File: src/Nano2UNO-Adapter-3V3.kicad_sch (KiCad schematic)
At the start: 13 parts, among them J1 ESW-108-33-L-S, J2 ESW-110-33-L-S, J3 ESW-108-33-L-S, J4 ESW-106-33-L-S, J5 PPPC151LFBN-RC, J6 PPPC151LFBN-RC, J7 TSW-103-15-L-D, J8 PJ-102A, SW1 1825910-6, U1 R-78K5.0-0.5

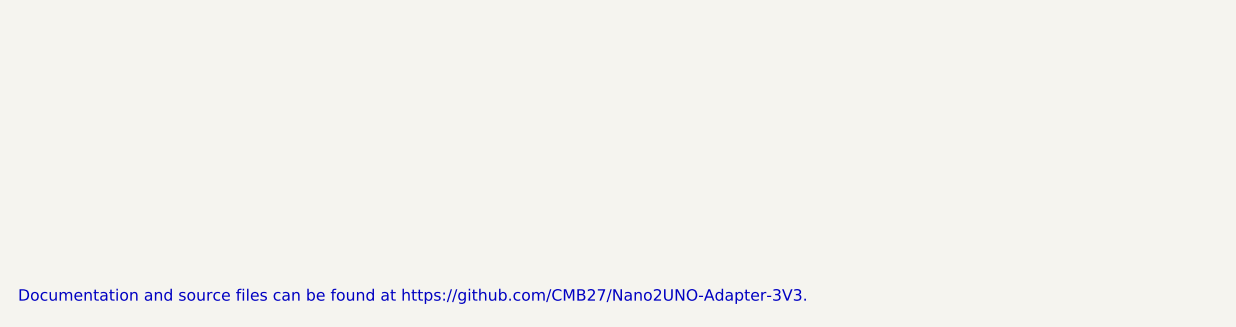
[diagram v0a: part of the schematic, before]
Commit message: Increased the font size of the comments and dimensions.
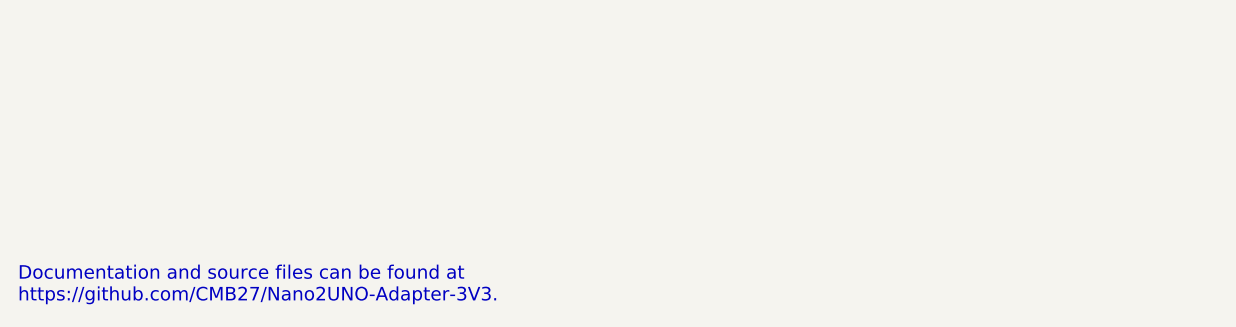
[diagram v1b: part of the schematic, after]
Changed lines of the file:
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@@
   (title_block
     (title "Nano2UNO Adapter 3V3")
-    (date "2023-12-02")
+    (date "2023-12-05")
     (rev "0.0.1")
     (company "Designer: C. M. Bulliner")
@@
     (stroke (width 0) (type default))
   )
-  (text "Documentation and source files can be found at https://github.com/CMB27/Nano2UNO-Adapter-3V3."
+  (text "Documentation and source files can be found at\nhttps://github.com/CMB27/Nano2UNO-Adapter-3V3."
     (at 15.24 200.66 0)
-    (effects (font (size 1.27 1.27)) (justify left bottom))
+    (effects (font (size 1.5 1.5)) (justify left bottom) (href "https://github.com/CMB27/Nano2UNO-Adapter-3V3"))
   )
   (label "D12{slash}CIPO" (at 167.64 50.8 0) (fields_autoplaced)
